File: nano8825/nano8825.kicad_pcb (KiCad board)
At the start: 2 copper layers, 75 x 90 mm, 24 parts, among them J1 Conn_01x02, J2 Conn_01x04, J3 Conn_01x04, J4 Conn_01x04, J5 Conn_01x02, J6 Conn_01x02, J7 Conn_01x02, J8 Conn_01x02_Female, SW1 SW_DIP_x03, SW2 SW_DIP_x03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

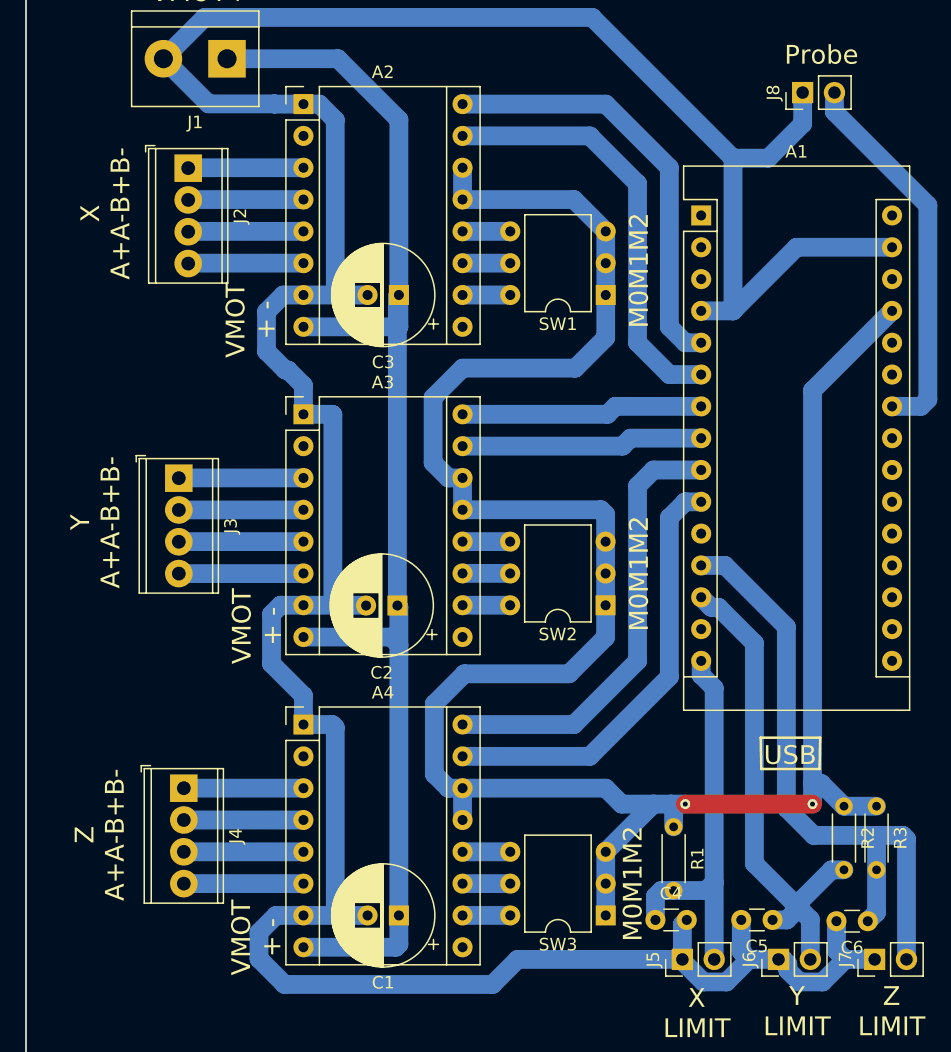
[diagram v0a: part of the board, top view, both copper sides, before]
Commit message: Renamed files
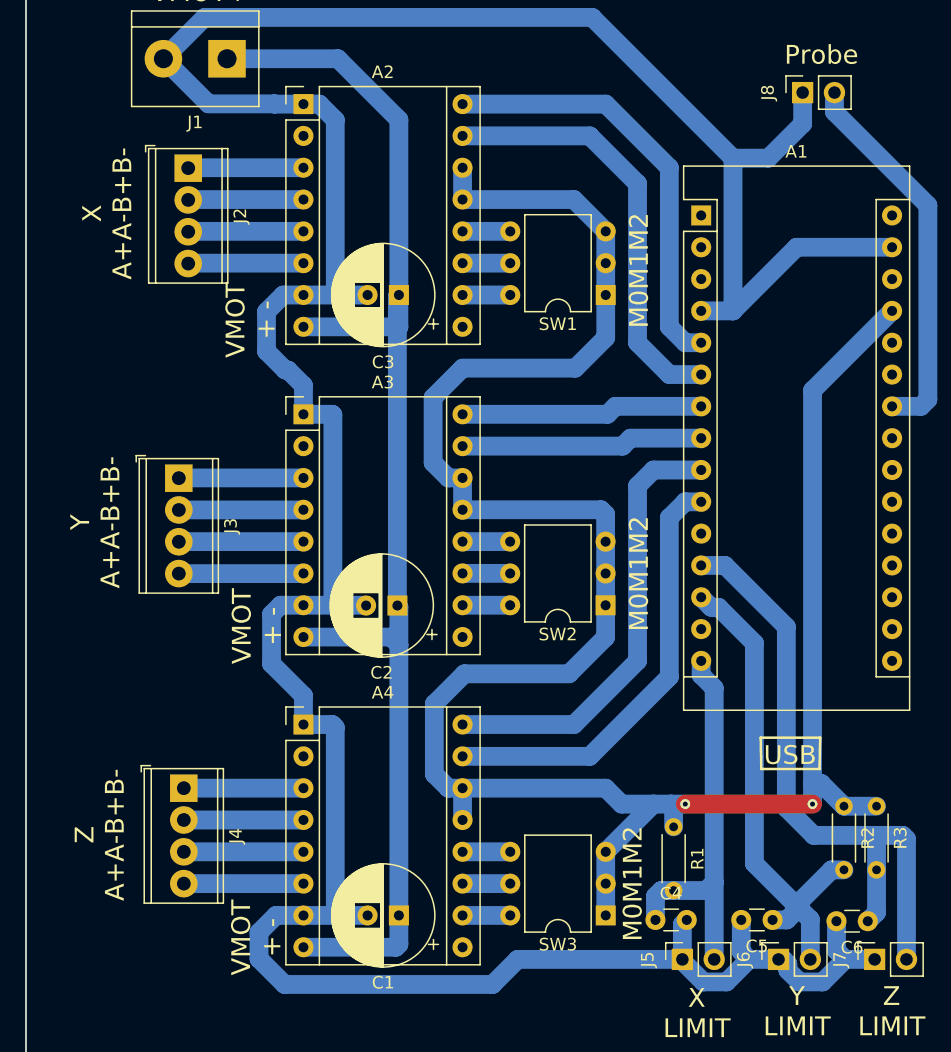
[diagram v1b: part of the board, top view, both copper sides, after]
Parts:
- J5, J6, J7, J8: footprint Connector_PinHeader_2.54mm:PinHeader_1x02_P2.54mm_Vertical -> Connector_PinSocket_2.54mm:PinSocket_1x02_P2.54mm_Vertical

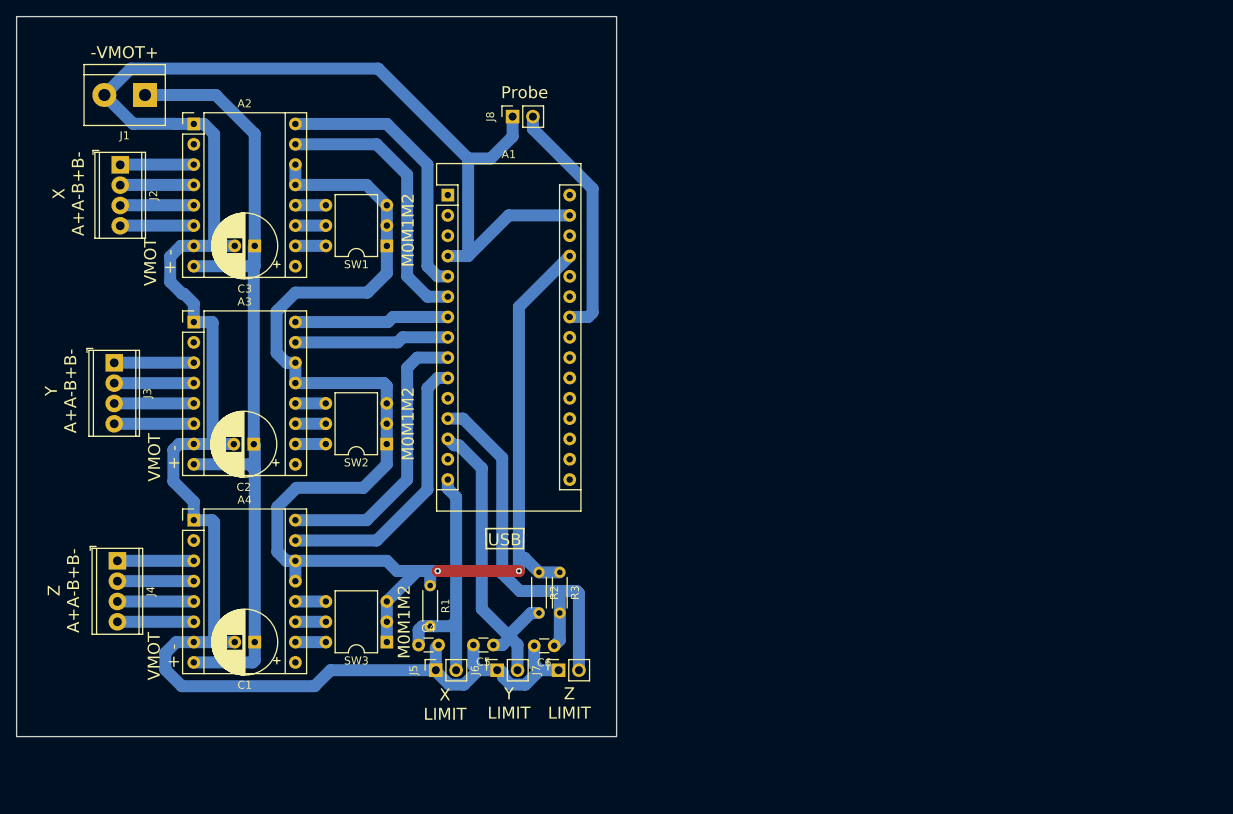
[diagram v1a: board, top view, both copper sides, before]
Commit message: Added Output for nano8825 board
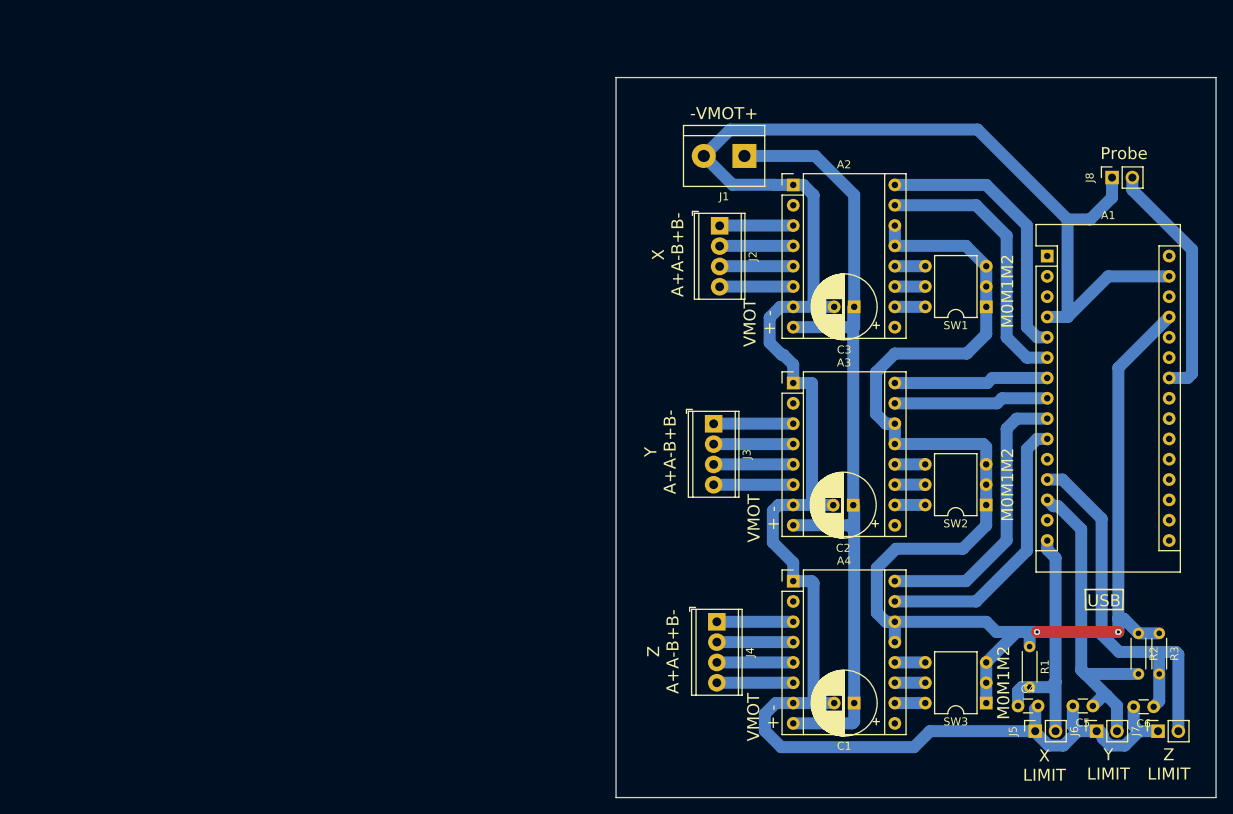
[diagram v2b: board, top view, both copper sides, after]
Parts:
- moved A1 75.3 mm to (163.8, 74.9)
- moved A2 75.3 mm to (132.1, 66.0)
- moved A3 75.3 mm to (132.1, 90.8)
- moved J1 75.3 mm to (126.0, 62.4)
- moved J4 75.3 mm to (122.5, 120.7)
- moved J8 75.3 mm to (171.9, 65.1)
- moved R3 75.3 mm to (177.8, 122.1)
- moved SW1 75.3 mm to (156.2, 81.3)
- moved SW3 75.3 mm to (156.2, 130.8)
- moved A4 75.3 mm to (132.1, 115.6)
- moved C1 75.3 mm to (139.7, 130.8)
- moved C2 75.3 mm to (139.6, 106.1)
- moved C3 75.3 mm to (139.7, 81.3)
- moved C4 75.3 mm to (160.2, 131.2)
- moved C5 75.3 mm to (169.5, 131.2)
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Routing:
- net Net-(A1-Pad13): track 40.5 -> 42.5 mm

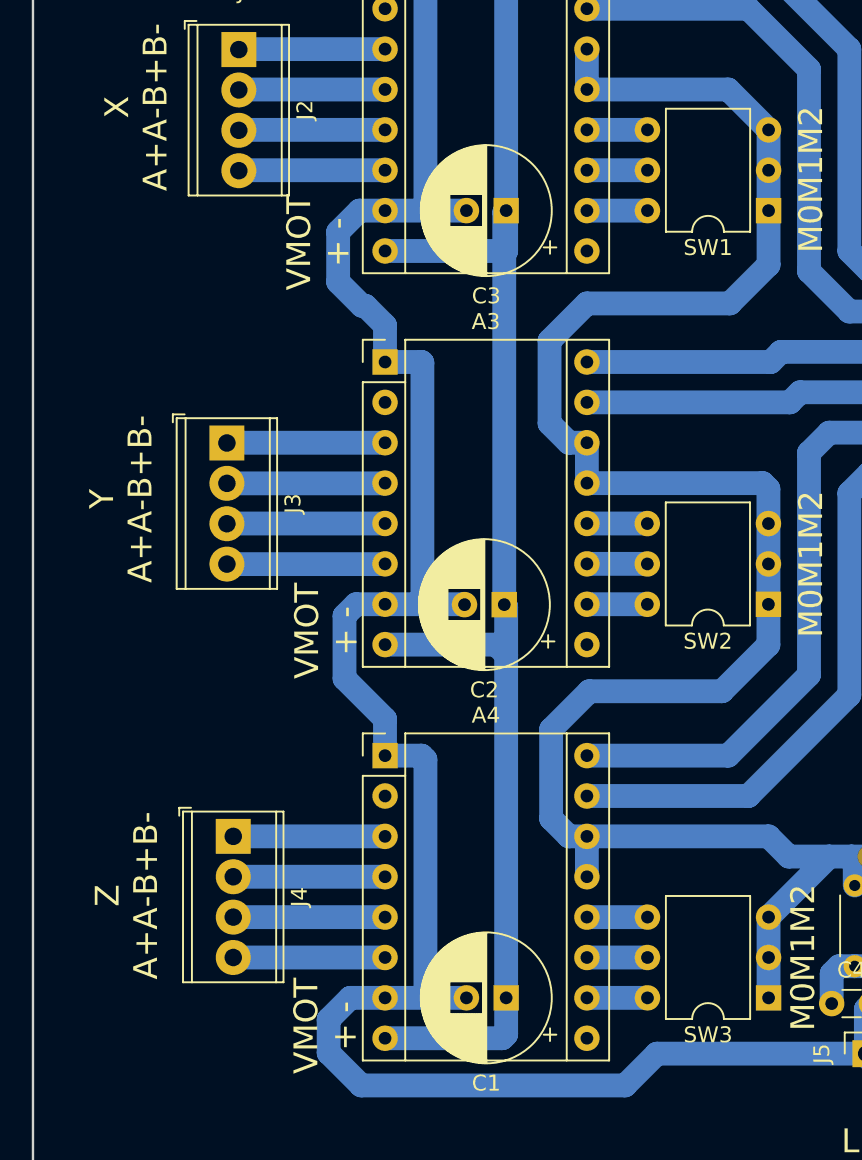
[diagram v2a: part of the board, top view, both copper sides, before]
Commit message: Updated some footprints
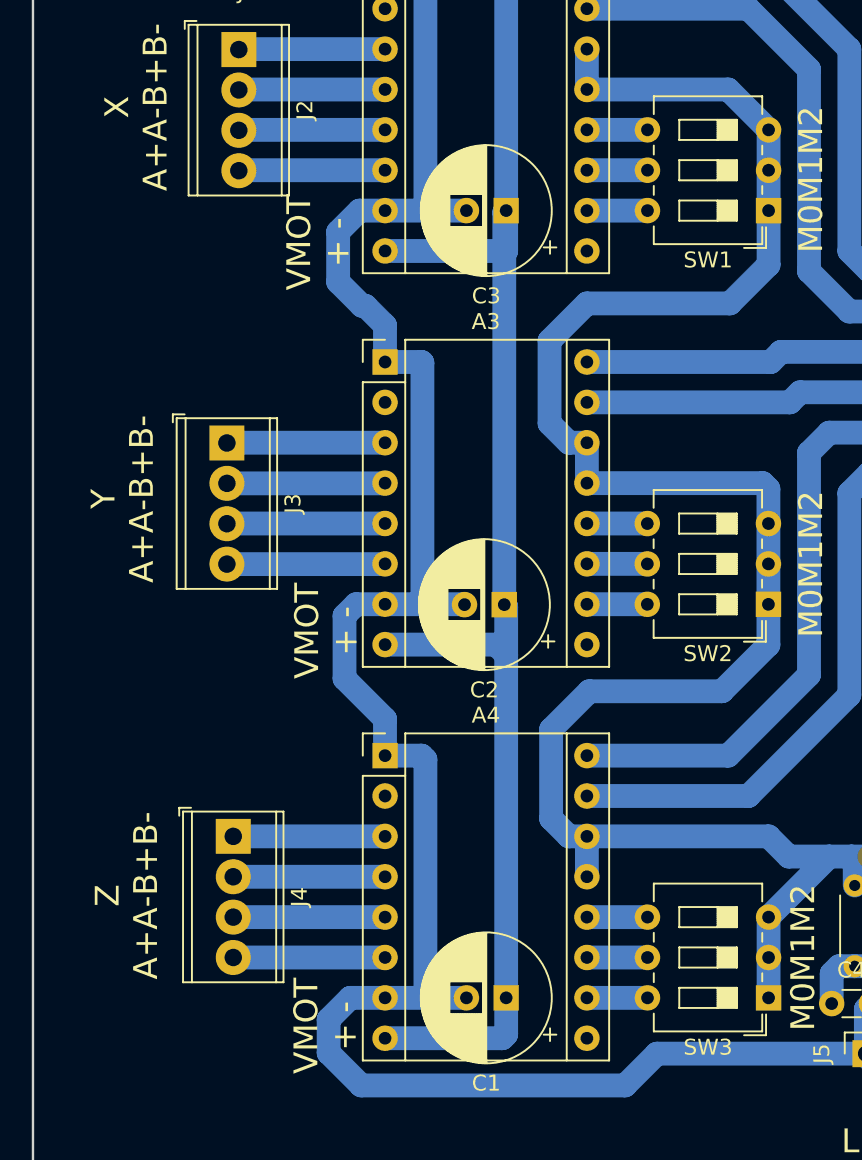
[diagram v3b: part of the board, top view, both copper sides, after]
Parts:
- SW1, SW2, SW3: footprint Package_DIP:DIP-6_W7.62mm -> Button_Switch_THT:SW_DIP_SPSTx03_Slide_6.7x9.18mm_W7.62mm_P2.54mm_LowProfile
